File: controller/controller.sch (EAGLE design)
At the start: 47 parts, among them IC1 MEGA8-P, IC2 FT230XS, IC3 LM50, T1 2N3904, X1 MINI-USB_SHIELD5P2-32005-601, Y1 32.768kHz

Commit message: Update
Completed the controller design
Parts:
- removed R12: 3k3, rcl:R-EU_0207/10
- removed R13: 10k, rcl:R-EU_0207/10
- added C11, C20: 100n, rcl:C-EU025-024X044
- added C19: 47u, rcl:CPOL-EUE1.8-4
- added R100, R101: 27, rcl:R-EU_R0603
- C12: value 4u7 -> 10n; device rcl:CPOL-EUE1.8-4 -> rcl:C-EU025-024X044
- C13: value 100n -> 470n
- C14, C15: value 10n -> 100n
- C16, C4: value 100n -> 10n
- C17: value 100n -> 4u7; device rcl:C-EU025-024X044 -> rcl:CPOL-EUE1.8-4
- C18: value 470n -> 47u; device rcl:C-EU025-024X044 -> rcl:CPOL-EUE1.8-4
- C5, C7: value 47u -> 100n; device rcl:CPOL-EUE1.8-4 -> rcl:C-EU025-024X044
- ISP1: value AVRISP-BOX -> AVRISP-6; device adafruit:AVRISP-BOX -> adafruit:AVRISP-6
- R10: value 100k -> 10k; device pot:TRIM_US-CT6 -> rcl:R-EU_0207/10
- R11: value Blue/White/Green=80/Amber=180 -> 100k; device rcl:R-EU_0207/10 -> pot:TRIM_US-CT6
- R2: value 27 -> 10k; device rcl:R-EU_R0603 -> rcl:R-EU_0207/10
- R3: value 27 -> 3k3; device rcl:R-EU_R0603 -> rcl:R-EU_0207/10
- R6: value 3k3 -> Blue/White/Green=80/Amber=180
- R7: value 3k3 -> 10k
- R8, R9: value 10k -> 3k3
- renumbered IC2 to IC101, IC3 to IC100, Q2 to Q1, X1 to USB
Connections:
- net N$12 renamed V_BUS
- net ADC1: now also R11.S; no longer R10.S
- net CONT: now also C13.1, R7.2; no longer C18.1, R13.2
- net E: now also IC1.PB5(SCK), ISP1.SCK; no longer IC1.PB4(MISO), ISP1.MISO
- net GND: now also C1.2, C10.2, C11.1, C12.2, C17.-, C18.-, C19.-, C2.1, C20.2, C3.2, C5.2, C7.2, C8.1, R11.A, S3.2; no longer C1.1, C10.1, C12.-, C17.2, C18.2, C2.2, C3.1, C5.-, C7.-, C8.2, R10.A, S3.1
- net INT0: now also R2.1, RTC.#INTA; no longer R8.2, RTC.SQW/#INTB
- net INT1: now also R10.2, RTC.SQW/#INTB; no longer R9.1, RTC.#INTA
- net LIGHT: now also R3.1; no longer R12.1
- net N$1: now also C2.2; no longer C1.2
- net N$10: now also R100.1; no longer R3.1
- net N$11: now also C11.2; no longer C10.2
- net N$18: now also R3.2; no longer R12.2
- net N$19: now also R6.2; no longer R11.2
- net N$2: now also C1.1; no longer C2.1
- net N$20: now also R9.2; no longer R7.2
- net N$21: now also R8.1; no longer R6.1
- net N$3: now also R100.2; no longer R3.2
- net N$4: now also C8.2; no longer C3.2
- net N$6: now also R101.1; no longer R2.1
- net N$7: now also S2.2; no longer S3.2
- net N$8: now also S1.2; no longer S2.2
- net N$9: now also R101.2; no longer R2.2
- net PWM: now also R7.1; no longer R13.1
- net RESET: now also C6.1, S3.1; no longer C4.1, S1.2
- net RS: now also IC1.PB4(MISO), ISP1.MISO; no longer IC1.PB5(SCK), ISP1.SCK
- net VCC: now also C10.1, C12.1, C17.+, C18.+, C19.+, C20.1, C3.1, C4.1, C5.1, C7.1, R10.1, R11.E, R2.2, R6.1, R8.2, R9.1; no longer C12.+, C13.1, C17.1, C5.+, C6.1, C7.+, C8.1, R10.E, R11.1, R6.2, R7.1, R8.1, R9.2
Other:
- moved on the sheet: C1, C10, C13, C14, C15, C16, C2, C3, C4, C6, C8, C9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

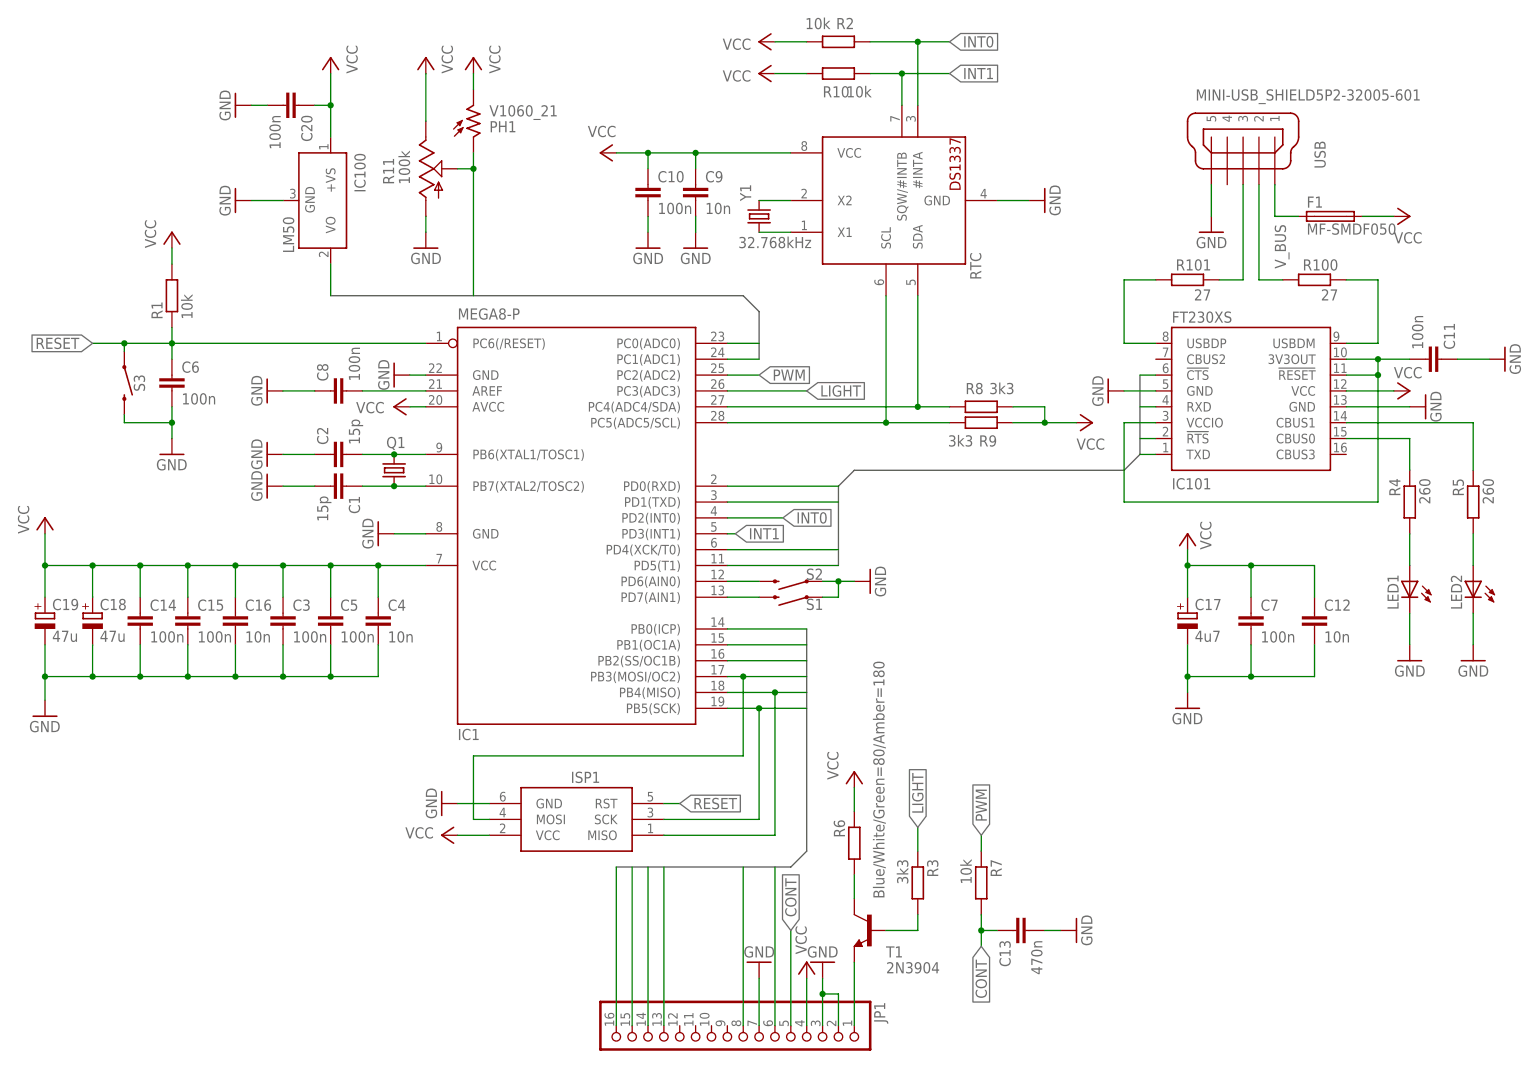
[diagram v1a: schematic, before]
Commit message: Update
Corrected some things and added partlist to the controller project
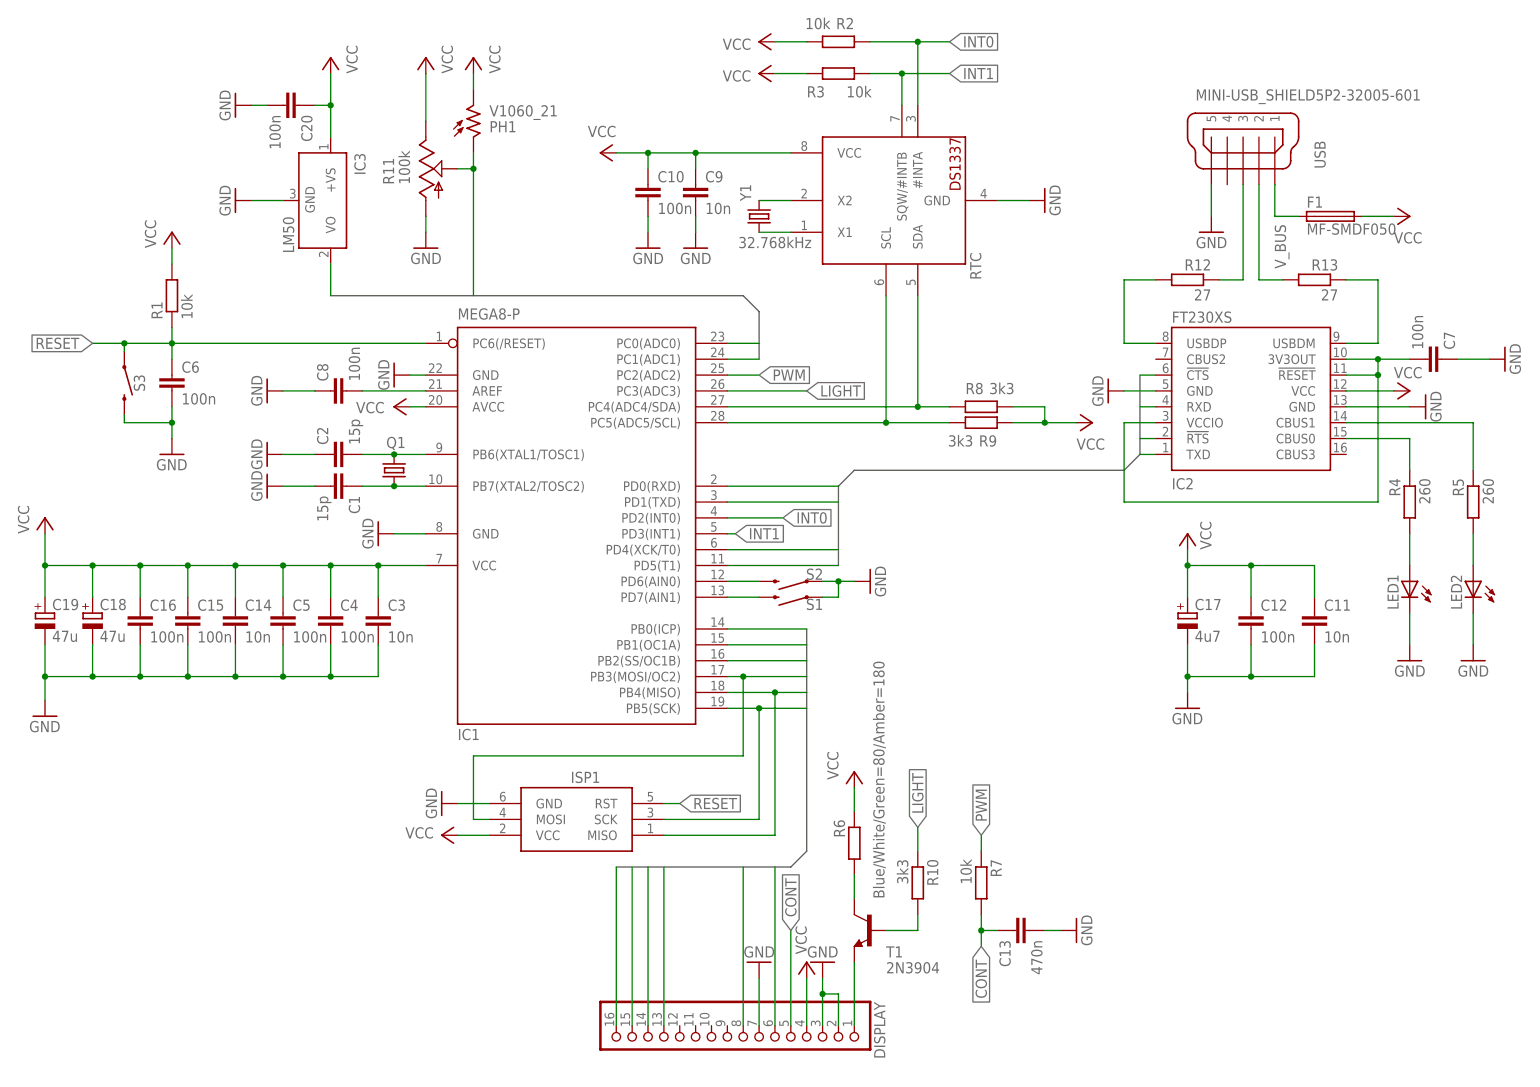
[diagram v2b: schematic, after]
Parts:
- C11, C14, C3: value 100n -> 10n
- C12, C16, C4: value 10n -> 100n
- R10: value 10k -> 3k3
- R3: value 3k3 -> 10k
- renumbered IC100 to IC3, IC101 to IC2, JP1 to DISPLAY, R100 to R13, R101 to R12
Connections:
- net GND: now also C11.2, C7.1; no longer C11.1, C7.2
- net INT1: now also R3.2; no longer R10.2
- net LIGHT: now also R10.1; no longer R3.1
- net N$11: now also C7.2; no longer C11.2
- net N$18: now also R10.2; no longer R3.2
- net VCC: now also C11.1, R3.1; no longer C7.1, R10.1
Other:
- moved on the sheet: C11, C12, C14, C16, C3, C4, C5, C7, R10, R3

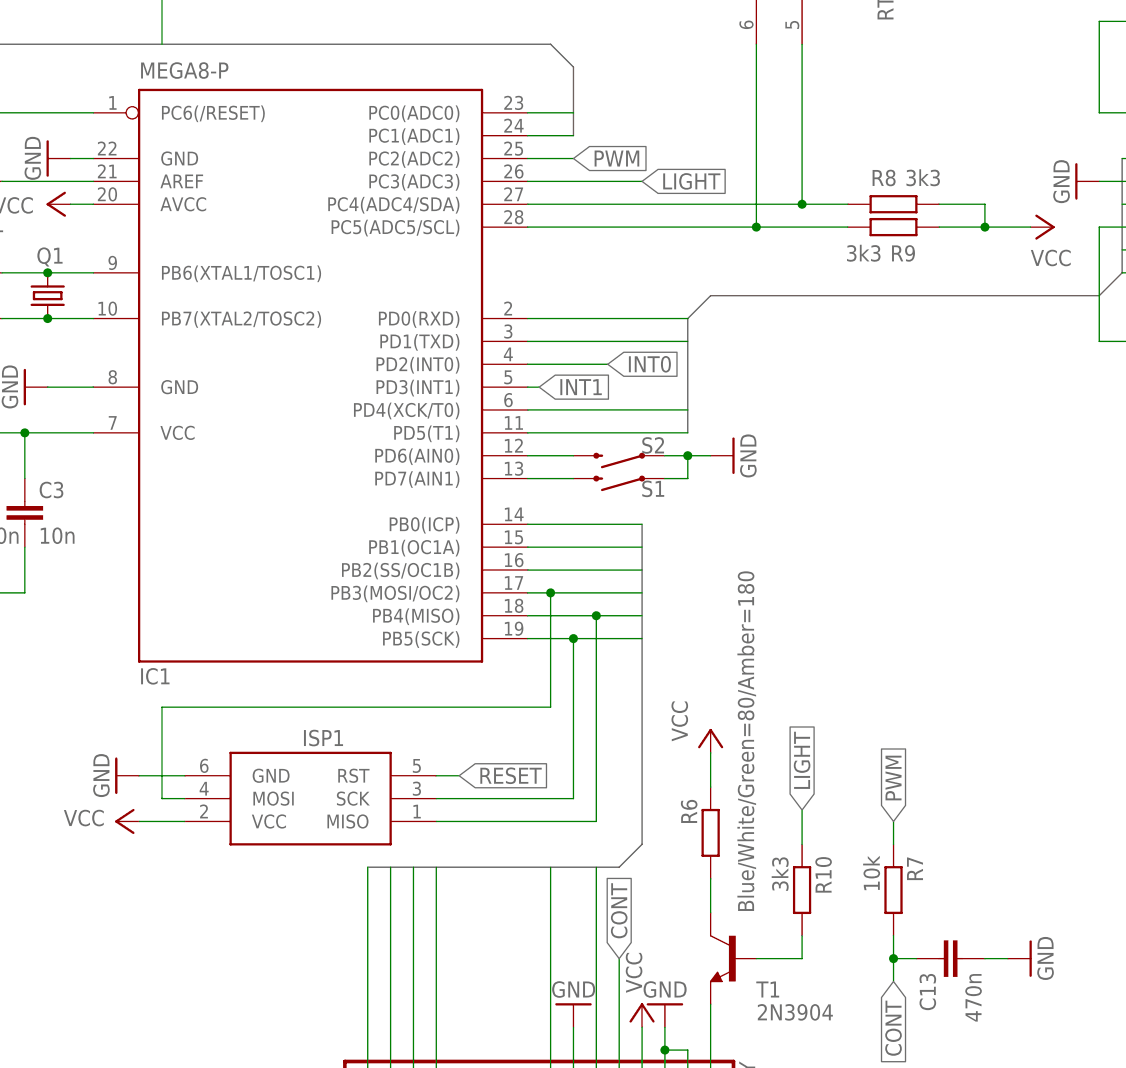
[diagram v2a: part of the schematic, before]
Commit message: Update
Corrected wrong direction of the display header
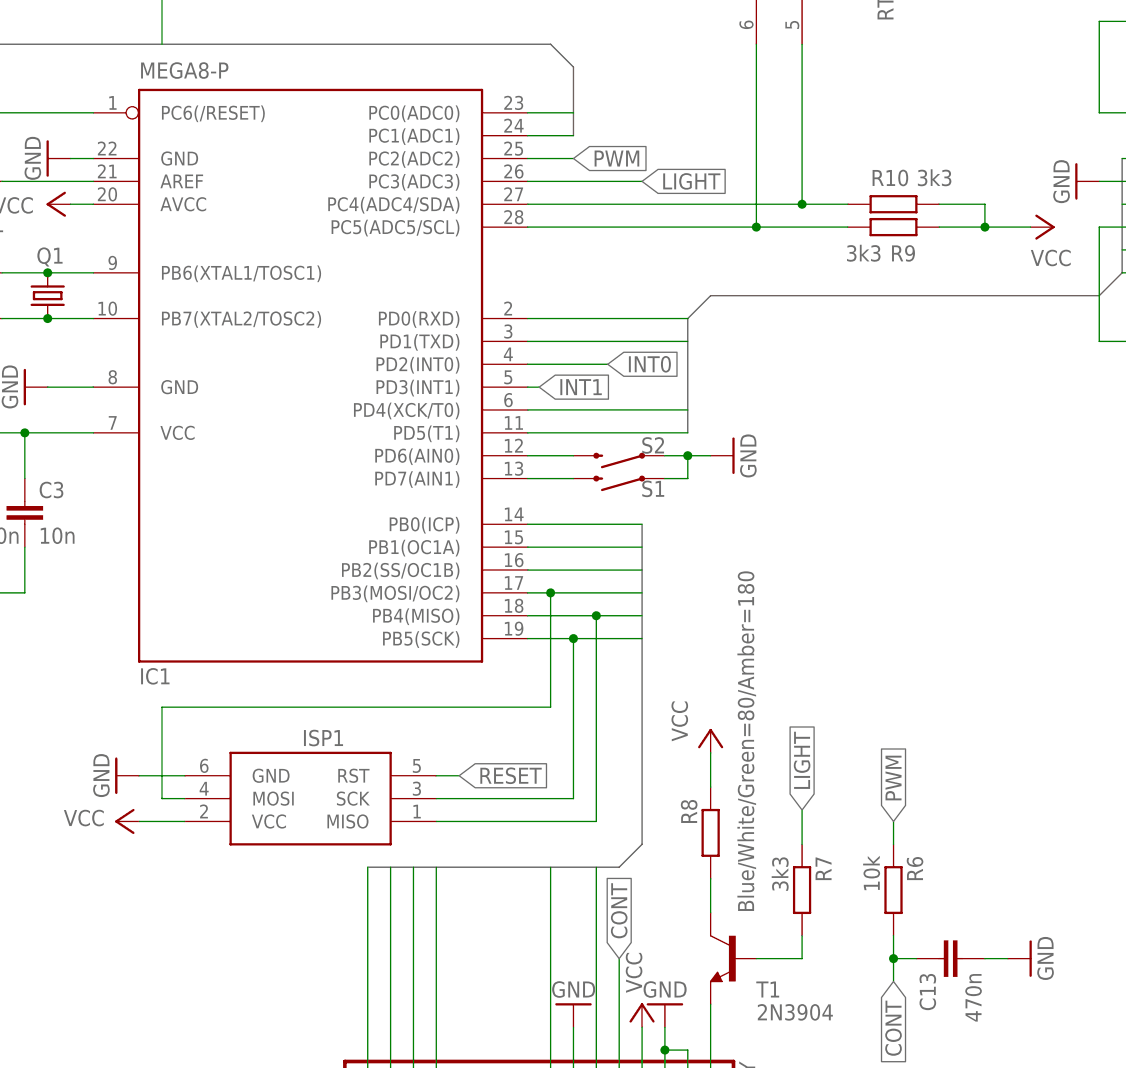
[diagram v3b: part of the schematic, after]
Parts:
- R6: value Blue/White/Green=80/Amber=180 -> 10k
- R7: value 10k -> 3k3
- R8: value 3k3 -> Blue/White/Green=80/Amber=180
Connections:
- net CONT: now also R6.2; no longer R7.2
- net DB4: now also IC1.PB3(MOSI/OC2), ISP1.MOSI; no longer IC1.PB0(ICP)
- net DB5: now also IC1.PB2(SS/OC1B); no longer IC1.PB1(OC1A)
- net DB6: now also IC1.PB1(OC1A); no longer IC1.PB2(SS/OC1B)
- net DB7: now also IC1.PB0(ICP); no longer IC1.PB3(MOSI/OC2), ISP1.MOSI
- net E: now also IC1.PB4(MISO), ISP1.MISO; no longer IC1.PB5(SCK), ISP1.SCK
- net LIGHT: now also R7.1; no longer R10.1
- net N$18: now also R7.2; no longer R10.2
- net N$19: now also R8.2; no longer R6.2
- net N$21: now also R10.1; no longer R8.1
- net PWM: now also R6.1; no longer R7.1
- net RS: now also IC1.PB5(SCK), ISP1.SCK; no longer IC1.PB4(MISO), ISP1.MISO
- net VCC: now also R10.2, R8.1; no longer R6.1, R8.2
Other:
- moved on the sheet: R10, R6, R7, R8
